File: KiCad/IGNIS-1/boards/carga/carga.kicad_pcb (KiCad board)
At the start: 2 copper layers, 62 x 62 mm, 12 parts, among them J1 LiPo_1S, J2 RBF_pin, J40 Backplane, SW1 Main_SW, U2 TPS63020, U40 TP4056

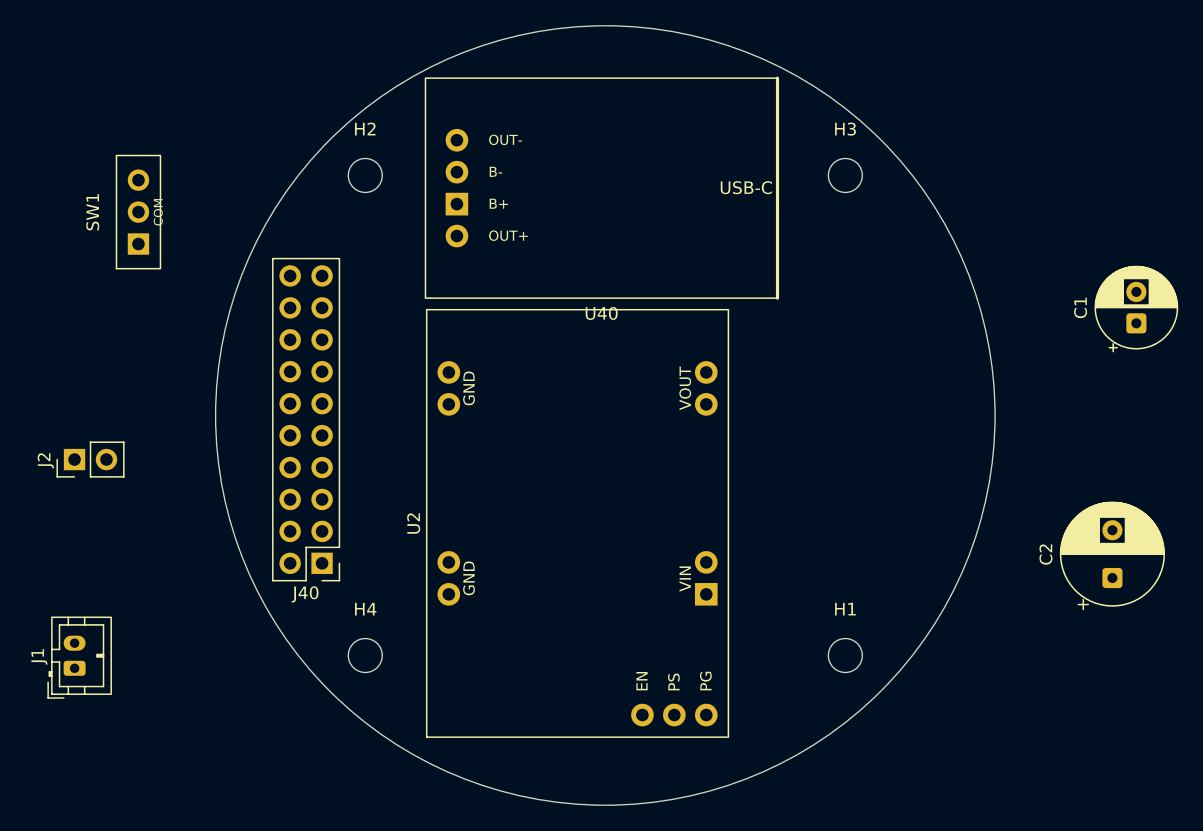
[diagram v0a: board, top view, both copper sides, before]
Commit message: 5 boards separados, falta ajustar dimensiones de BME280 y MQ-135
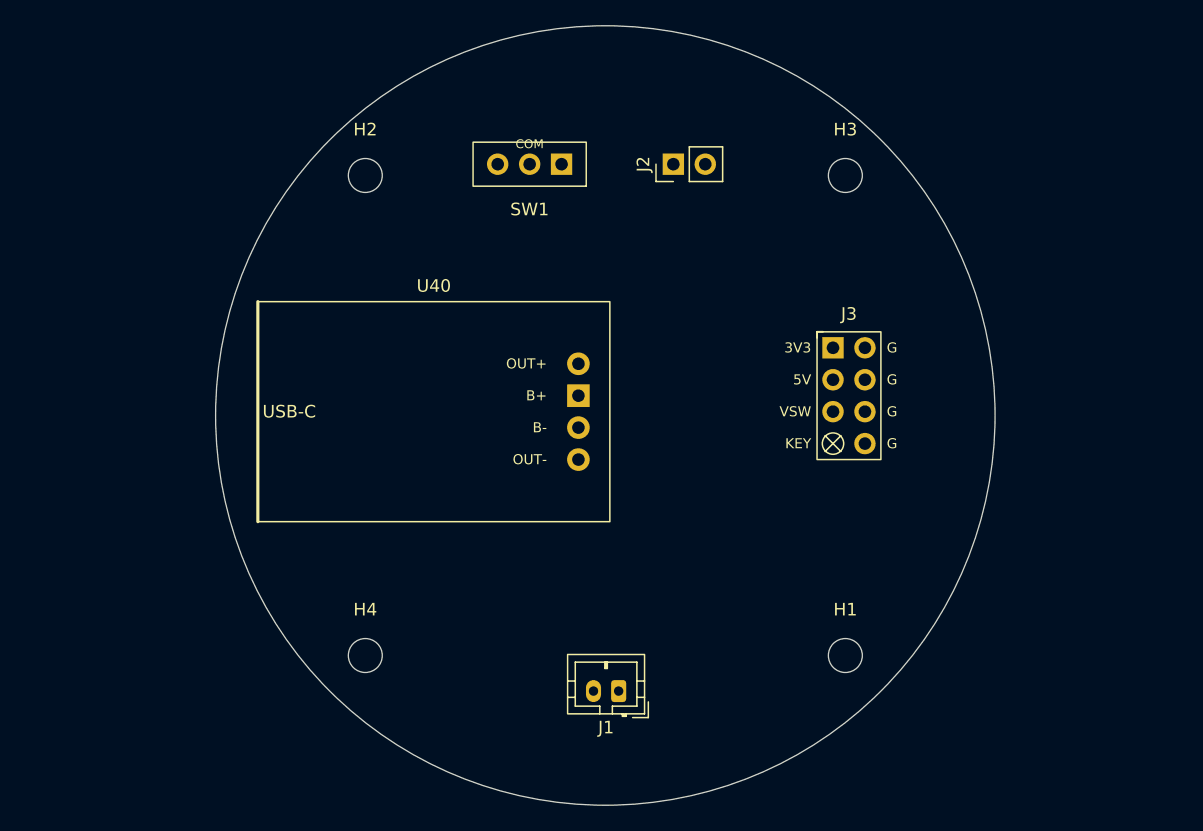
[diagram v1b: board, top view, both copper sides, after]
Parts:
- removed C1: 22uF, Capacitor_THT:CP_Radial_D6.3mm_P2.50mm
- removed C2: 100uF, Capacitor_THT:CP_Radial_D8.0mm_P3.80mm
- removed J40: Backplane, Connector_PinHeader_2.54mm:PinHeader_2x10_P2.54mm_Vertical
- removed U2: TPS63020, IGNIS1:TPS63020_module
- added J3: J_PWR_2x4, IGNIS1:J_PWR_2x4_Keyed, F.Cu at (119.4, 98.4)
- moved J2 53.1 mm to (105.4, 80.0)
- moved J1 43.3 mm to (101.1, 121.9), turned to 180 degrees
- moved SW1 31.3 mm to (94.0, 80.0), turned to 180 degrees
- moved U40 22.2 mm to (86.4, 99.7), turned to 0 degrees

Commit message: Se agregaron tracks. PCB Cerebro libre de errores.
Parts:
- moved J2 2.54 mm to (108.0, 80.0), turned to -90 degrees
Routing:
- net GND: track 0.00 -> 75.6 mm
- net VSW: track 0.00 -> 51.4 mm
- net BATT: track 0.00 -> 24.8 mm
- net VBAT_P: track 0.00 -> 20.1 mm
- net VRBF: track 0.00 -> 8.89 mm
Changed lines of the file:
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@@
 	(footprint "Connector_PinHeader_2.54mm:PinHeader_1x02_P2.54mm_Vertical"
 		(layer "F.Cu")
-		(at 105.41 80.01 90)
+		(at 107.95 80.01 -90)
 		(descr "Through hole straight pin header, 1x02, 2.54mm pitch, single row")
 		(tags "Through hole pin header THT 1x02 2.54mm single row")
@@
 		(duplicate_pad_numbers_are_jumpers no)
 		(fp_line
+			(start -1.38 3.92)
+			(end 1.38 3.92)
+			(stroke
+				(width 0.12)
+				(type solid)
+			)
+			(layer "F.SilkS")
+		)
+		(fp_line
+			(start -1.38 1.27)
+			(end -1.38 3.92)
+			(stroke
+				(width 0.12)
+				(type solid)
+			)
+			(layer "F.SilkS")
+		)
+		(fp_line
+			(start -1.38 1.27)
+			(end 1.38 1.27)
+			(stroke
+				(width 0.12)
+				(type solid)
+			)
+			(layer "F.SilkS")
+		)
+		(fp_line
+			(start 1.38 1.27)
+			(end 1.38 3.92)
+			(stroke
+				(width 0.12)
+				(type solid)
+			)
+			(layer "F.SilkS")
+		)
+		(fp_line
+			(start -1.38 0)
+			(end -1.38 -1.38)
+			(stroke
+				(width 0.12)
+				(type solid)
+			)
+			(layer "F.SilkS")
+		)
+		(fp_line
 			(start -1.38 -1.38)
 			(end 0 -1.38)
-			(stroke
-				(width 0.12)
-				(type solid)
-			)
-			(layer "F.SilkS")
-		)
-		(fp_line
-			(start -1.38 0)
-			(end -1.38 -1.38)
-			(stroke
-				(width 0.12)
-				(type solid)
-			)
-			(layer "F.SilkS")
-		)
-		(fp_line
-			(start 1.38 1.27)
-			(end 1.38 3.92)
-			(stroke
-				(width 0.12)
-				(type solid)
-			)
-			(layer "F.SilkS")
-		)
-		(fp_line
-			(start -1.38 1.27)
-			(end 1.38 1.27)
-			(stroke
-				(width 0.12)
-				(type solid)
-			)
-			(layer "F.SilkS")
-		)
-		(fp_line
-			(start -1.38 1.27)
-			(end -1.38 3.92)
-			(stroke
-				(width 0.12)
-				(type solid)
-			)
-			(layer "F.SilkS")
-		)
-		(fp_line
-			(start -1.38 3.92)
-			(end 1.38 3.92)
 			(stroke
 				(width 0.12)
@@
 		)
 		(fp_line
+			(start -1.27 3.81)
+			(end -1.27 -0.635)
+			(stroke
+				(width 0.1)
+				(type solid)
+			)
+			(layer "F.Fab")
+		)
+		(fp_line
+			(start 1.27 3.81)
+			(end -1.27 3.81)
+			(stroke
+				(width 0.1)
+				(type solid)
+			)
+			(layer "F.Fab")
+		)
+		(fp_line
+			(start -1.27 -0.635)
+			(end -0.635 -1.27)
+			(stroke
+				(width 0.1)
+				(type solid)
+			)
+			(layer "F.Fab")
+		)
+		(fp_line
+			(start -0.635 -1.27)
+			(end 1.27 -1.27)
+			(stroke
+				(width 0.1)
+				(type solid)
+			)
+			(layer "F.Fab")
+		)
+		(fp_line
 			(start 1.27 -1.27)
 			(end 1.27 3.81)
@@
 			(layer "F.Fab")
 		)
-		(fp_line
-			(start -0.635 -1.27)
-			(end 1.27 -1.27)
-			(stroke
-				(width 0.1)
-				(type solid)
-			)
-			(layer "F.Fab")
-		)
-		(fp_line
-			(start -1.27 -0.635)
-			(end -0.635 -1.27)
-			(stroke
-				(width 0.1)
-				(type solid)
-			)
-			(layer "F.Fab")
-		)
-		(fp_line
-			(start 1.27 3.81)
-			(end -1.27 3.81)
-			(stroke
-				(width 0.1)
-				(type solid)
-			)
-			(layer "F.Fab")
-		)
-		(fp_line
-			(start -1.27 3.81)
-			(end -1.27 -0.635)
-			(stroke
-				(width 0.1)
-				(type solid)
-			)
-			(layer "F.Fab")
-		)
 		(fp_text user "${REFERENCE}"
 			(at 0 1.27 0)
@@
 		)
 		(pad "1" thru_hole rect
-			(at 0 0 90)
+			(at 0 0 270)
 			(size 1.7 1.7)
 			(drill 1)
@@
 		)
 		(pad "2" thru_hole circle
-			(at 0 2.54 90)
+			(at 0 2.54 270)
 			(size 1.7 1.7)
 			(drill 1)
@@
 		(layer "Edge.Cuts")
 	)
+	(segment
+		(start 107.95 128.27)
+		(end 107.95 114.935)
+		(width 0.25)
+		(layer "F.Cu")
+		(net "GND")
+	)
+	(segment
+		(start 97.86 103.505)
+		(end 97.86 120.72)
+		(width 0.25)
+		(layer "F.Cu")
+		(net "GND")
+	)
+	(segment
+		(start 120.65 99.695)
+		(end 120.65 97.155)
+		(width 0.25)
+		(layer "F.Cu")
+		(net "GND")
+	)
+	(segment
+		(start 120.65 94.615)
+		(end 120.65 97.155)
+		(width 0.25)
+		(layer "F.Cu")
+		(net "GND")
+	)
+	(segment
+		(start 99.06 121.92)
+		(end 99.06 128.27)
+		(width 0.25)
+		(layer "F.Cu")
+		(net "GND")
+	)
+	(segment
+		(start 97.86 103.505)
+		(end 97.86 100.965)
+		(width 0.25)
+		(layer "F.Cu")
+		(net "GND")
+	)
+	(segment
+		(start 97.86 120.72)
+		(end 99.06 121.92)
+		(width 0.25)
+		(layer "F.Cu")
+		(net "GND")
+	)
+	(segment
+		(start 99.06 128.27)
+		(end 107.95 128.27)
+		(width 0.25)
+		(layer "F.Cu")
+		(net "GND")
+	)
+	(segment
+		(start 120.65 102.235)
+		(end 120.65 99.695)
+		(width 0.25)
+		(layer "F.Cu")
+		(net "GND")
+	)
+	(segment
+		(start 107.95 114.935)
+		(end 120.65 102.235)
+		(width 0.25)
+		(layer "F.Cu")
+		(net "GND")
+	)
+	(segment
+		(start 113.665 95.25)
+		(end 118.11 99.695)
+		(width 0.25)
+		(layer "F.Cu")
+		(net "VSW")
+	)
+	(segment
+		(start 113.665 74.93)
+		(end 113.665 95.25)
+		(width 0.25)
+		(layer "F.Cu")
+		(net "VSW")
+	)
+	(segment
+		(start 93.98 80.01)
+		(end 93.98 74.93)
+		(width 0.25)
+		(layer "F.Cu")
+		(net "VSW")
+	)
+	(segment
+		(start 93.98 74.93)
+		(end 113.665 74.93)
+		(width 0.25)
+		(layer "F.Cu")
+		(net "VSW")
+	)
+	(segment
+		(start 96.52 80.01)
+		(end 105.41 80.01)
+		(width 0.25)
+		(layer "F.Cu")
+		(net "VRBF")
+	)
+	(segment
+		(start 107.95 80.01)
+		(end 107.95 85.795)
+		(width 0.25)
+		(layer "F.Cu")
+		(net "VBAT_P")
+	)
+	(segment
+		(start 107.95 85.795)
+		(end 97.86 95.885)
+		(width 0.25)
+		(layer "F.Cu")
+		(net "VBAT_P")
+	)
+	(segment
+		(start 97.86 98.425)
+		(end 101.06 101.625)
+		(width 0.25)
+		(layer "F.Cu")
+		(net "BATT")
+	)
+	(segment
+		(start 101.06 101.625)
+		(end 101.06 121.92)
+		(width 0.25)
+		(layer "F.Cu")
+		(net "BATT")
+	)
 	(embedded_fonts no)

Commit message: Todos los boards pasan el check, tracks completos
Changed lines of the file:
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@@
 		(descr "SS-12D00 SPDT slide switch, 3 pins inline P2.54. Pad2=common (center). Use as SPST on/off with symbol SW_SPST (pin1->pad1 throw, pin2->pad2 common); pad3 = other throw (unused).")
 		(property "Reference" "SW1"
-			(at 0 -3.6 0)
+			(at 3.683 -2.921 0)
 			(layer "F.SilkS")
 			(effects
@@
 		)
 		(property "Value" "Main_SW"
-			(at 0 3.6 0)
+			(at 3.683 3.048 0)
 			(layer "F.Fab")
 			(effects
@@
 		)
 		(fp_text user "COM"
-			(at 0 1.6 0)
-			(layer "F.SilkS")
-			(effects
-				(font
-					(size 0.7 0.7)
+			(at 0 -3.175 0)
+			(layer "F.SilkS")
+			(effects
+				(font
+					(size 0.8 0.8)
 					(thickness 0.12)
 				)
@@
 		)
 		(fp_text user "USB-C"
-			(at -11.5 0 0)
-			(layer "F.SilkS")
-			(effects
+			(at -10.922 -0.254 0)
+			(layer "F.SilkS")
+			(effects
